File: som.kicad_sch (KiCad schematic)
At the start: 39 parts, among them J10 Conn_FFC_Molex_5051101097, M1 Jetson-Nano-new-release, M2 jetson-nano-module, T2 BSS138PW, T4 BSS138PW, T5 BSS138PW

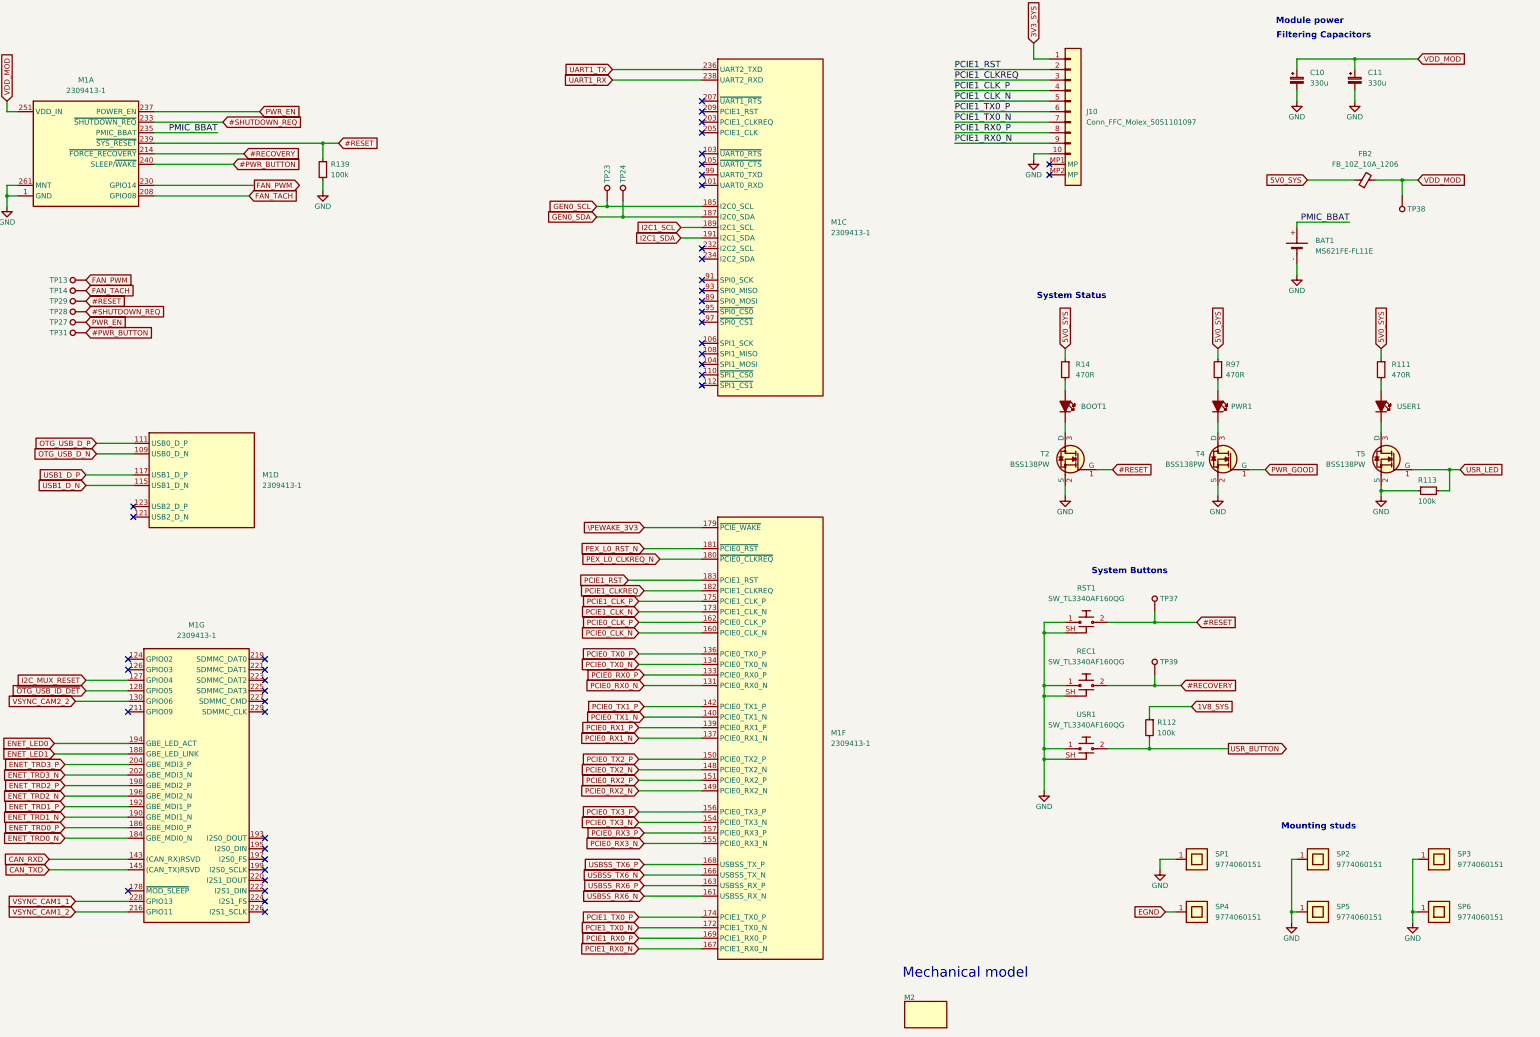
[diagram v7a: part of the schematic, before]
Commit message: [#56834] Fix components links
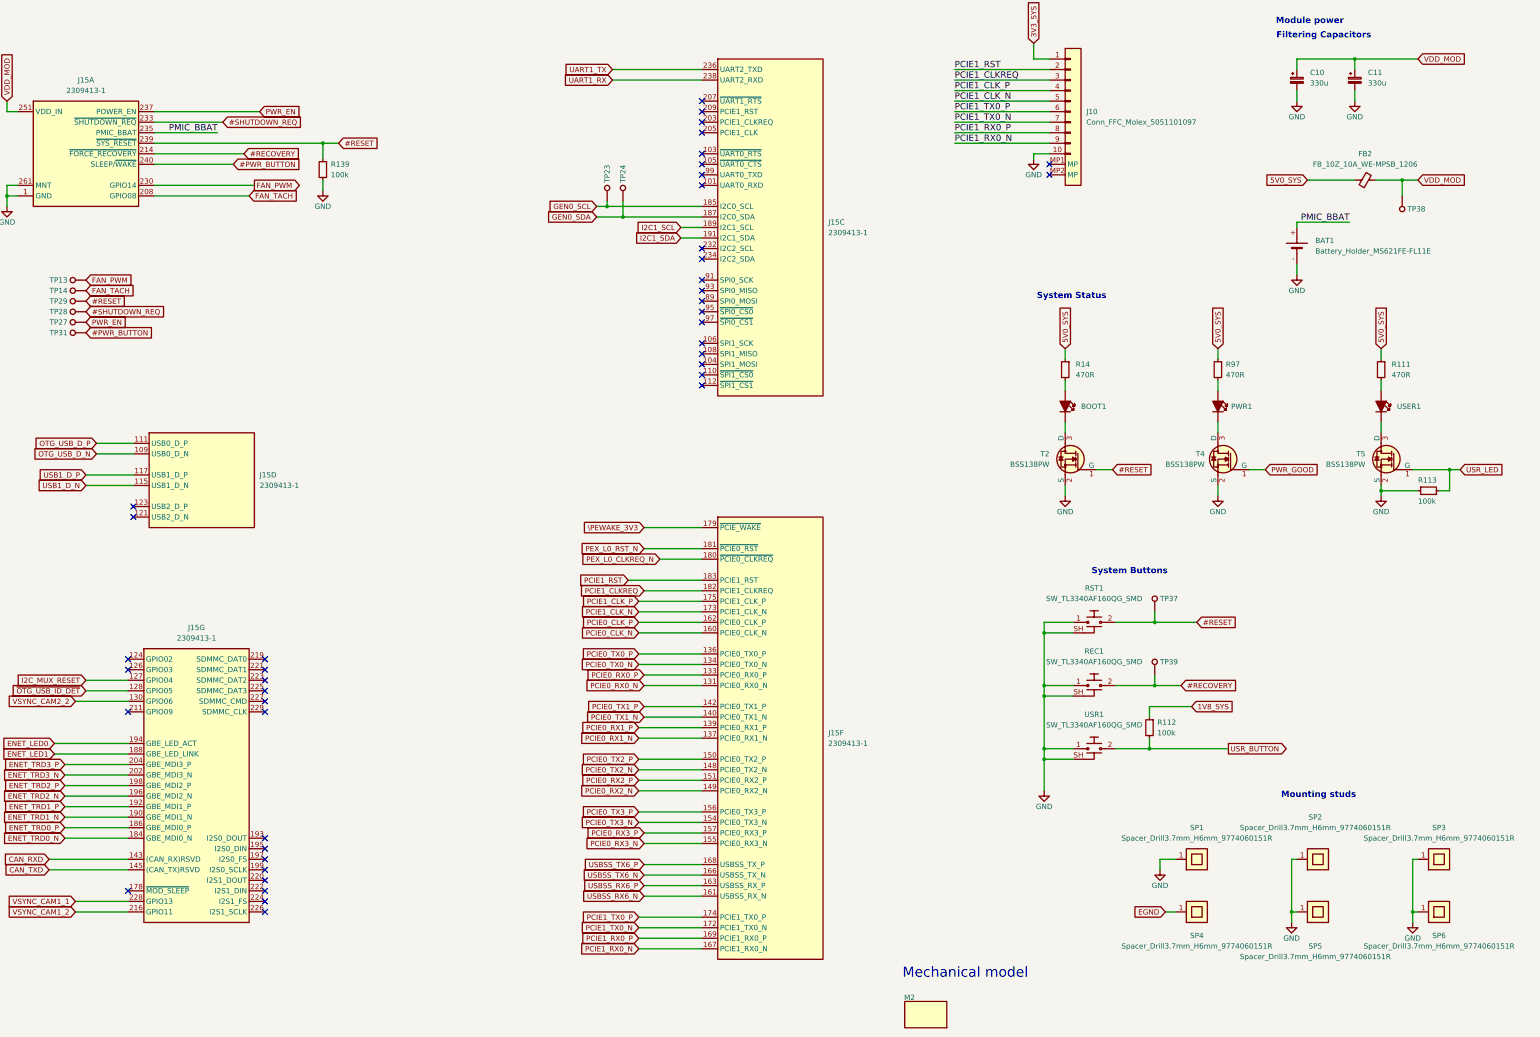
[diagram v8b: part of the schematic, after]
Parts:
- BAT1: value MS621FE-FL11E -> Battery_Holder_MS621FE-FL11E; footprint antmicro-footprints:MS621FE-FL11E -> jetson-nano-baseboard-footprints:MS621FE-FL11E; symbol antmicroBatteryHoldersClipsContacts:Battery_Holder_MS621FE-FL11E -> jetson-nano-baseboard:Battery_Holder_MS621FE-FL11E; Manufacturer Seiko -> Seiko Instruments
- BOOT1, PWR1, USER1: value ~ -> LED_G_0603_LG_L29K-G2J1-24-Z; footprint antmicro-footprints:LED_0603_1608Metric_G -> jetson-nano-baseboard-footprints:LED_0603_1608Metric_G; symbol antmicroLEDIndicationDiscrete:LED_G_0603_LG_L29K-G2J1-24-Z -> jetson-nano-baseboard:LED_G_0603_LG_L29K-G2J1-24-Z; Manufacturer Osram -> OSRAM
- C10, C11: value C_330u_KEMET_B -> C_Pol_330u_6.3V_KEMET-T520-B; footprint antmicro-footprints:KEMET_B -> jetson-nano-baseboard-footprints:C_Pol_EIA-B; symbol antmicroCapacitorspol:C_330u_KEMET_B -> jetson-nano-baseboard:C_Pol_330u_6.3V_KEMET-T520-B; Voltage (none) -> 6.3V
- FB2: value FB_10Z_10A_1206 -> FB_10Z_10A_WE-MPSB_1206; footprint antmicro-footprints:FB_1206_3216Metric -> jetson-nano-baseboard-footprints:FB_1206_3216Metric; symbol antmicroFerriteBeadsandChips:FB_10Z_10A_1206 -> jetson-nano-baseboard:FB_10Z_10A_WE-MPSB_1206
- J10: footprint antmicro-footprints:Conn_FFC_Molex_5051101097 -> jetson-nano-baseboard-footprints:Conn_FFC_Molex_5051101097; symbol antmicroFCCConnectors:Conn_FFC_Molex_5051101097 -> jetson-nano-baseboard:Conn_FFC_Molex_5051101097
- J15: renamed from M1; value Jetson-Nano-new-release -> Bus_DDR4_SODIMM_CUSTOM_Jetson-Nano-H9.2mm-socket; footprint antmicro-footprints:TE_2309413 -> jetson-nano-baseboard-footprints:TE_2309413; symbol antmicroSoMConnectors:Jetson-Nano-new-release -> jetson-nano-baseboard:Bus_DDR4_SODIMM_CUSTOM_Jetson-Nano-H9.2mm-socket
- M2: value jetson-nano-module -> Jetson-Nano; footprint antmicro-footprints:jetson-nano-module-5.2H -> jetson-nano-baseboard-footprints:Module_Jetson-Nano; symbol antmicroModules:jetson-nano-module -> jetson-nano-baseboard:Jetson-Nano; Manufacturer NVIDIA -> Nvidia
- R111, R14, R97: footprint antmicro-footprints:R_0402_1005Metric -> jetson-nano-baseboard-footprints:R_0402_1005Metric; symbol antmicroResistors0402:R_470R_0402 -> jetson-nano-baseboard:R_470R_0402
- R112, R113, R139: footprint antmicro-footprints:R_0402_1005Metric -> jetson-nano-baseboard-footprints:R_0402_1005Metric; symbol antmicroResistors0402:R_100k_0402 -> jetson-nano-baseboard:R_100k_0402
- REC1, RST1, USR1: value SW_TL3340AF160QG -> SW_TL3340AF160QG_SMD; footprint antmicro-footprints:SW_TL3340AF160QG -> jetson-nano-baseboard-footprints:SW_TL3340AF160QG_SMD; symbol antmicroPushbuttonSwitches:SW_TL3340AF160QG -> jetson-nano-baseboard:SW_TL3340AF160QG_SMD
- SP1, SP2, SP3, SP4, SP5, SP6: value 9774060151 -> Spacer_Drill3.7mm_H6mm_9774060151R; footprint antmicro-footprints:Spacer_SMD_M2.5_H6mm_Wurth_9774060151 -> jetson-nano-baseboard-footprints:Spacer_Drill3.7mm_H6mm_9774060151R; symbol antmicroMechanicalParts:Spacer_H6mm_9774060151 -> jetson-nano-baseboard:Spacer_Drill3.7mm_H6mm_9774060151R; MPN 9774060151 -> 9774060151R
- T2, T4, T5: footprint antmicro-footprints:SC70-3 -> jetson-nano-baseboard-footprints:SC70-3; symbol antmicroTransistorsFETsMOSFETsSingle:BSS138PW -> jetson-nano-baseboard:BSS138PW
- TP13, TP14, TP23, TP24, TP27, TP28, TP29, TP31, TP37, TP38, TP39: footprint antmicro-footprints:TP_SMD_1.5mm -> jetson-nano-baseboard-footprints:TP_SMD_1.5mm; symbol antmicroTestPoints:TP_1.5mm_SMD -> jetson-nano-baseboard:TP_1.5mm_SMD; MPN N/A -> (none); Manufacturer N/A -> (none)
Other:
- moved on the sheet: REC1, RST1, USR1
